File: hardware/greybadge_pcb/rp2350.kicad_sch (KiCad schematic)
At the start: 35 parts, among them J6 USB_C_Receptacle_USB2.0, SW10 SW_Push, SW9 SW_Push, U6 W25Q128JVS, U7 RP2350_60QFN, Y1 12Mhz

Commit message: Fix prev commit
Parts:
- renumbered J6 to J5, R28 to R27, R29 to R28, R30 to R29, R31 to R30, R32 to R31, R33 to R32, R34 to R33, R35 to R34, R36 to R35, R37 to R36

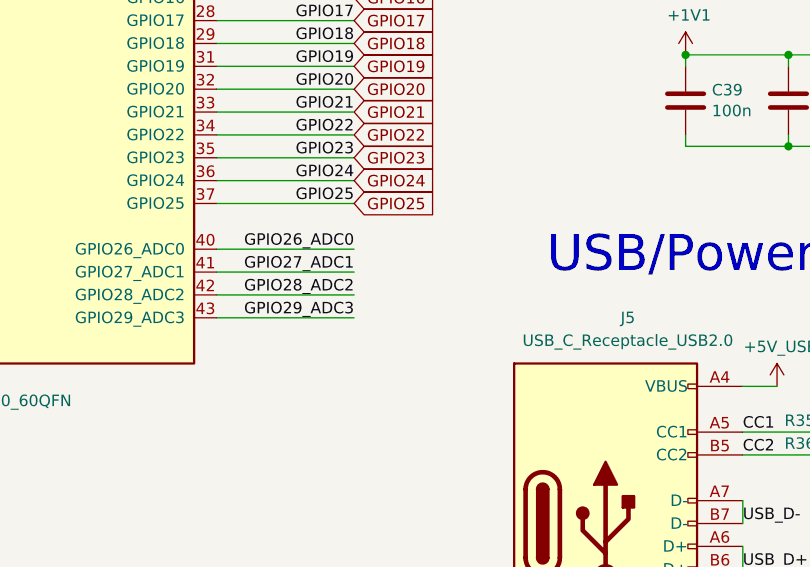
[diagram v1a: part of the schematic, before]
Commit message: Route ADC and power, cleanup routing/silkscreen
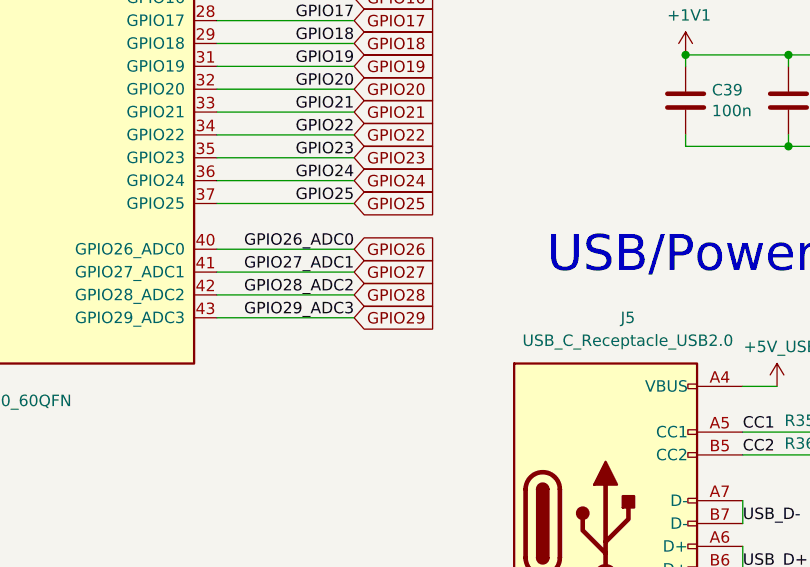
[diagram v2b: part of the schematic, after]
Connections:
- net GPIO26_ADC0 renamed GPIO26
- net GPIO27_ADC1 renamed GPIO27
- net GPIO28_ADC2 renamed GPIO28
- net GPIO29_ADC3 renamed GPIO29
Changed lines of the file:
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@@
+		)
+	)
+	(global_label "GPIO29"
+		(shape input)
+		(at 162.56 138.43 0)
+		(fields_autoplaced yes)
+		(effects
+			(font
+				(size 1.27 1.27)
+			)
+			(justify left)
+		)
+		(property "Intersheetrefs" "${INTERSHEET_REFS}"
+			(at 172.4395 138.43 0)
+			(effects
+				(font
+					(size 1.27 1.27)
+				)
+				(justify left)
+				(hide yes)
+			)
 		)
 	)
@@
 		)
 	)
+	(global_label "GPIO27"
+		(shape input)
+		(at 162.56 133.35 0)
+		(fields_autoplaced yes)
+		(effects
+			(font
+				(size 1.27 1.27)
+			)
+			(justify left)
+		)
+		(property "Intersheetrefs" "${INTERSHEET_REFS}"
+			(at 172.4395 133.35 0)
+			(effects
+				(font
+					(size 1.27 1.27)
+				)
+				(justify left)
+				(hide yes)
+			)
+		)
+	)
+	(global_label "GPIO26"
+		(shape input)
+		(at 162.56 130.81 0)
+		(fields_autoplaced yes)
+		(effects
+			(font
+				(size 1.27 1.27)
+			)
+			(justify left)
+		)
+		(property "Intersheetrefs" "${INTERSHEET_REFS}"
+			(at 172.4395 130.81 0)
+			(effects
+				(font
+					(size 1.27 1.27)
+				)
+				(justify left)
+				(hide yes)
+			)
+		)
+	)
 	(global_label "GPIO9"
 		(shape input)
@@
 			(effects
 				(font
+					(size 1.27 1.27)
+				)
+				(justify left)
+				(hide yes)
+			)
+		)
+	)
+	(global_label "GPIO28"
+		(shape input)
+		(at 162.56 135.89 0)
+		(fields_autoplaced yes)
+		(effects
+			(font
+				(size 1.27 1.27)
+			)
+			(justify left)
+		)
+		(property "Intersheetrefs" "${INTERSHEET_REFS}"
+			(at 172.4395 135.89 0)
+			(effects
+				(font

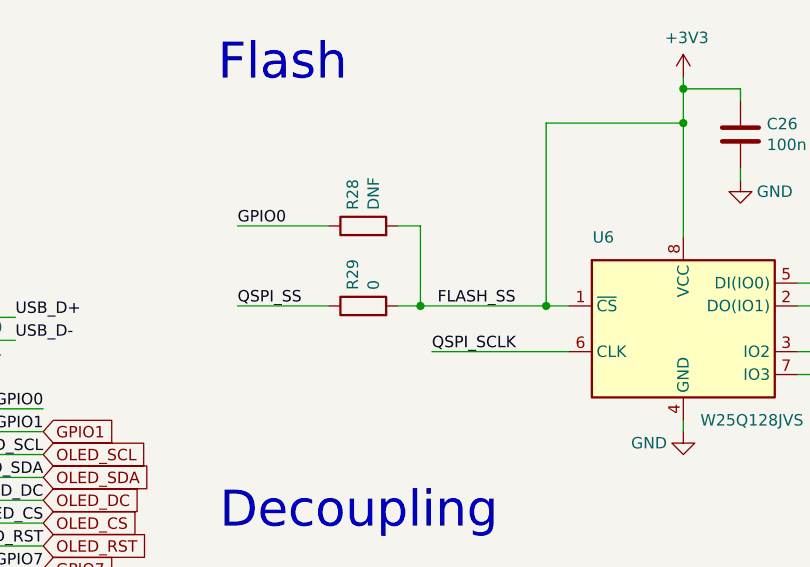
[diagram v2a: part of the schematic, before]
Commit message: fix: rp2350 flash
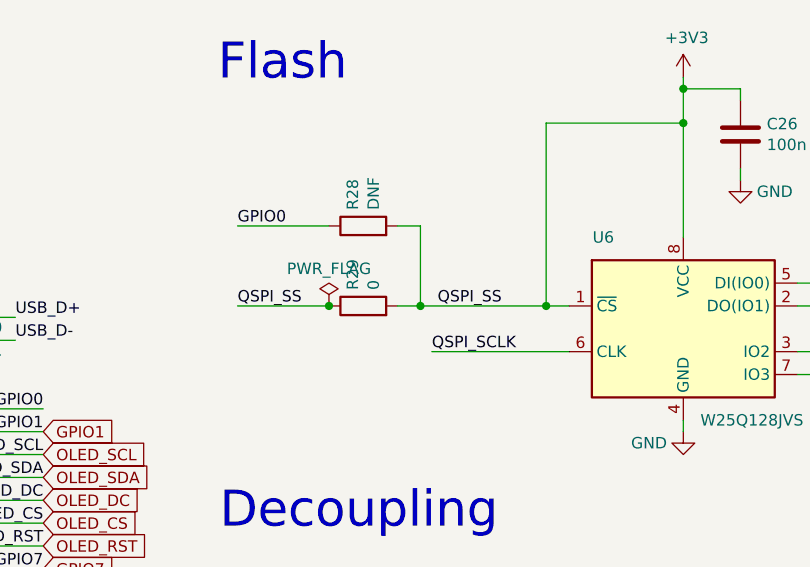
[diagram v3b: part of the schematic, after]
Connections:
- net QSPI_SS is gone; now on net +3V3: R29.1, R32.1, U7.60 (QSPI_SS)
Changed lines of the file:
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@@
 	)
 	(junction
+		(at 194.31 50.8)
+		(diameter 0)
+		(color 0 0 0 0)
+	)
+	(junction
 		(at 25.4 45.72)
 		(diameter 0)
@@
 		)
 	)
-	(label "FLASH_SS"
+	(label "QSPI_SS"
 		(at 206.375 50.8 0)
 		(effects
@@
 					(unit 1)
 				)
+			)
+		)
+	)
+	(symbol
+		(lib_id "power:PWR_FLAG")
+		(at 194.31 50.8 0)
+		(unit 1)
+		(exclude_from_sim no)
+		(in_bom yes)
+		(on_board yes)
+		(dnp no)
+		(fields_autoplaced yes)
+		(property "Reference" "#FLG05"
+			(at 194.31 48.895 0)
+			(effects
+				(font
+					(size 1.27 1.27)
+				)
+				(hide yes)
+			)
+		)
+		(property "Value" "PWR_FLAG"
+			(at 194.31 46.6669 0)
+			(effects
+				(font
+					(size 1.27 1.27)
+				)
+			)
+		)
+		(property "Footprint" ""
+			(at 194.31 50.8 0)
+			(effects
+				(font
+					(size 1.27 1.27)
+				)
+				(hide yes)
+			)
+		)
+		(property "Datasheet" "~"
+			(at 194.31 50.8 0)
+			(effects
+				(font
+					(size 1.27 1.27)
+				)
+				(hide yes)
+			)
+		)
+		(property "Description" "Special symbol for telling ERC where power comes from"
+			(at 194.31 50.8 0)
+			(effects
+				(font
+					(size 1.27 1.27)
+				)
+				(hide yes)
+			)
+		)
+		(pin "1"
+		)
+		(instances
+			(project ""
+				(path "/4eb7ff30-5b75-4e83-8e37-4e6cd7a9e830/9563b0f2-de2f-44b6-a21c-14dec17cccec"
+					(reference "#FLG05")
+					(unit 1)
+				)

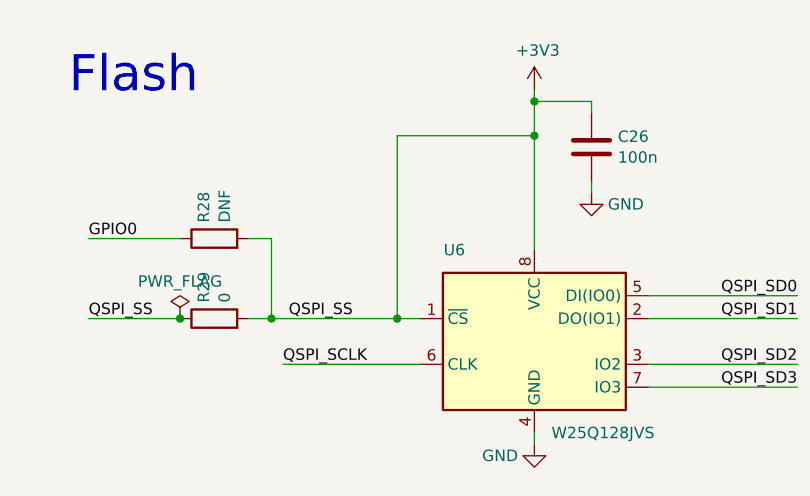
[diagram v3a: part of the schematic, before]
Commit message: feat: rp2350 schematic update for flash
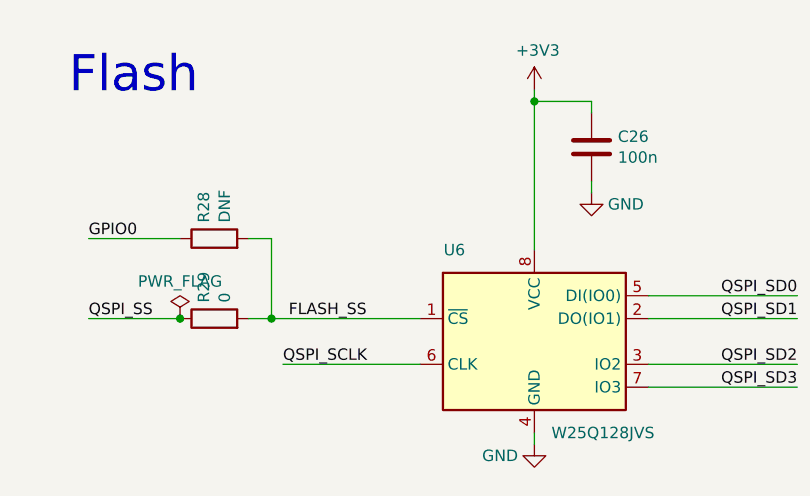
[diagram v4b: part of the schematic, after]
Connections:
- net +3V3: no longer R28.2, R29.1, R29.2, R32.1, U6.1 (~{CS}), U7.60 (QSPI_SS)
- new net FLASH_SS: R28.2, R29.2, U6.1 (~{CS})
- new net QSPI_SS: R29.1, R32.1, U7.60 (QSPI_SS)
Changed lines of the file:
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@@
-	)
-	(junction
-		(at 218.44 50.8)
-		(diameter 0)
-		(color 0 0 0 0)
 	)
 	(junction
@@
 	(junction
 		(at 119.38 41.91)
-		(diameter 0)
-		(color 0 0 0 0)
-	)
-	(junction
-		(at 233.68 30.48)
 		(diameter 0)
 		(color 0 0 0 0)
@@
 	(wire
 		(pts
-			(xy 233.68 26.67) (xy 233.68 30.48)
-		)
-		(stroke
-			(width 0)
-			(type default)
-		)
-	)
-	(wire
-		(pts
 			(xy 114.3 44.45) (xy 114.3 41.91)
 		)
@@
 	(wire
 		(pts
-			(xy 204.47 50.8) (xy 218.44 50.8)
+			(xy 204.47 50.8) (xy 220.98 50.8)
 		)
 		(stroke
@@
 	(wire
 		(pts
-			(xy 233.68 30.48) (xy 233.68 43.18)
+			(xy 233.68 26.67) (xy 233.68 43.18)
 		)
 		(stroke
@@
 	(wire
 		(pts
-			(xy 218.44 30.48) (xy 218.44 50.8)
-		)
-		(stroke
-			(width 0)
-			(type default)
-		)
-	)
-	(wire
-		(pts
 			(xy 149.6087 54.61) (xy 147.32 54.61)
 		)
@@
 	(wire
 		(pts
-			(xy 218.44 50.8) (xy 220.98 50.8)
-		)
-		(stroke
-			(width 0)
-			(type default)
-		)
-	)
-	(wire
-		(pts
 			(xy 25.4 62.23) (xy 25.4 66.04)
 		)
@@
 		(pts
 			(xy 303.022 81.28) (xy 303.022 85.5472)
-		)
-		(stroke
-			(width 0)
-			(type default)
-		)
-	)
-	(wire
-		(pts
-			(xy 218.44 30.48) (xy 233.68 30.48)
 		)
 		(stroke
@@
 		)
 	)
-	(label "QSPI_SS"
+	(label "FLASH_SS"
 		(at 206.375 50.8 0)
 		(effects
